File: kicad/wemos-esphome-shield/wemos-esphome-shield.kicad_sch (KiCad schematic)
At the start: 27 parts, among them Q1 2N2222, Q2 2N2222, Q3 2N2222, T1 Transformer_1P_1S, U1 WeMos_D1_mini

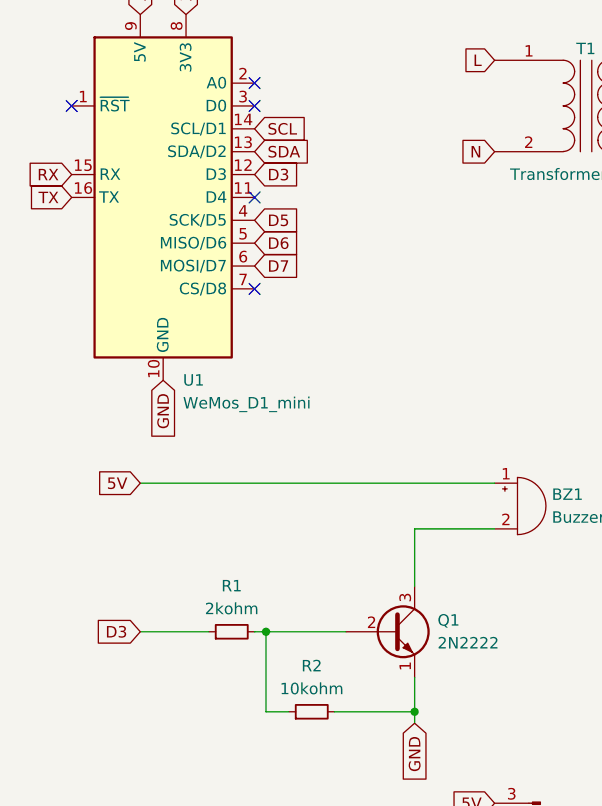
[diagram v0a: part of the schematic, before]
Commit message: reroute buzzer to D8
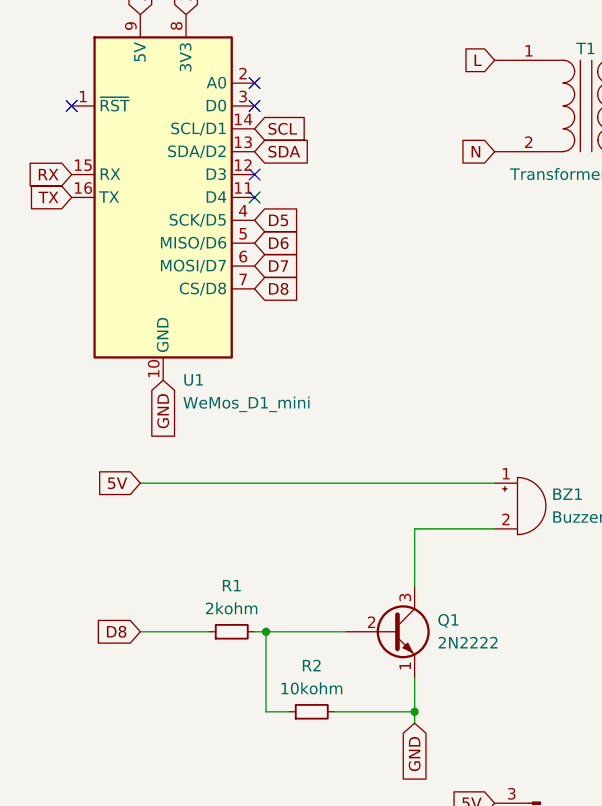
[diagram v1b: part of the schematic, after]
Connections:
- net D8: now reaches U1.7 (CS/D8)
- net D8: now also R1.1
- net D3: no longer names the net of U1.12 (D3)
- net D3: no longer R1.1
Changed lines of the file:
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@@
   (no_connect (at 55.88 40.64))
   (no_connect (at 55.88 30.48))
-  (no_connect (at 55.88 50.8))
+  (no_connect (at 55.88 38.1))
   (no_connect (at 193.04 68.58))
   (no_connect (at 193.04 55.88))
@@
     )
   )
-  (global_label "D3" (shape input) (at 55.88 38.1 0) (fields_autoplaced)
-    (effects (font (size 1.27 1.27)) (justify left))
-    (property "Intersheetrefs" "${INTERSHEET_REFS}" (at 60.7726 38.0206 0)
-      (effects (font (size 1.27 1.27)) (justify left) hide)
-    )
-  )
   (global_label "5V" (shape input) (at 193.04 24.13 180) (fields_autoplaced)
     (effects (font (size 1.27 1.27)) (justify right))
@@
     )
   )
+  (global_label "D8" (shape input) (at 55.88 50.8 0) (fields_autoplaced)
+    (effects (font (size 1.27 1.27)) (justify left))
+    (property "Intersheetrefs" "${INTERSHEET_REFS}" (at 61.3447 50.8 0)
+      (effects (font (size 1.27 1.27)) (justify left) hide)
+    )
+  )
   (global_label "D6" (shape input) (at 55.88 45.72 0) (fields_autoplaced)
     (effects (font (size 1.27 1.27)) (justify left))
@@
     )
   )
-  (global_label "D3" (shape input) (at 43.18 88.9 180) (fields_autoplaced)
-    (effects (font (size 1.27 1.27)) (justify right))
-    (property "Intersheetrefs" "${INTERSHEET_REFS}" (at 38.2874 88.8206 0)
-      (effects (font (size 1.27 1.27)) (justify right) hide)
-    )
+  (global_label "D8" (shape input) (at 43.18 88.9 180) (fields_autoplaced)
+    (effects (font (size 1.27 1.27)) (justify right))
+    (property "Intersheetrefs" "${INTERSHEET_REFS}" (at 37.7153 88.9 0)
+      (effects (font (size 1.27 1.27)) (justify right) hide)
+    )

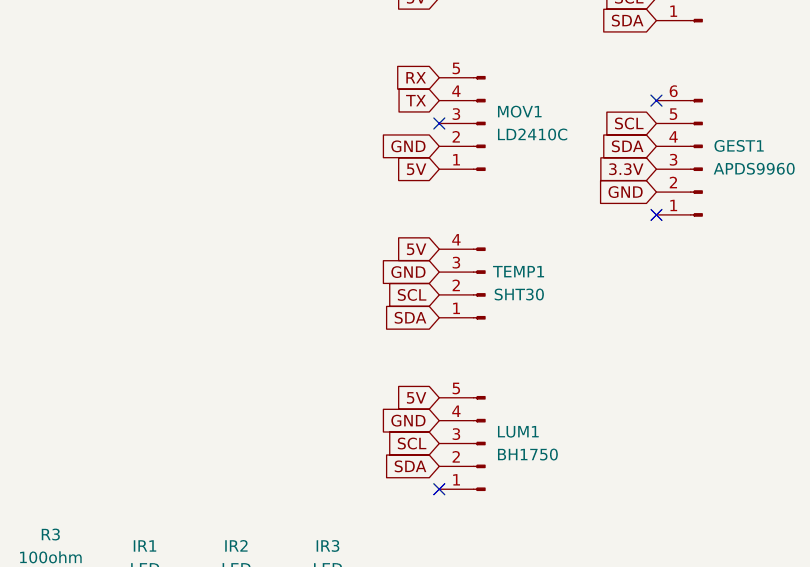
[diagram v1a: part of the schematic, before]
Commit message: move stuff around
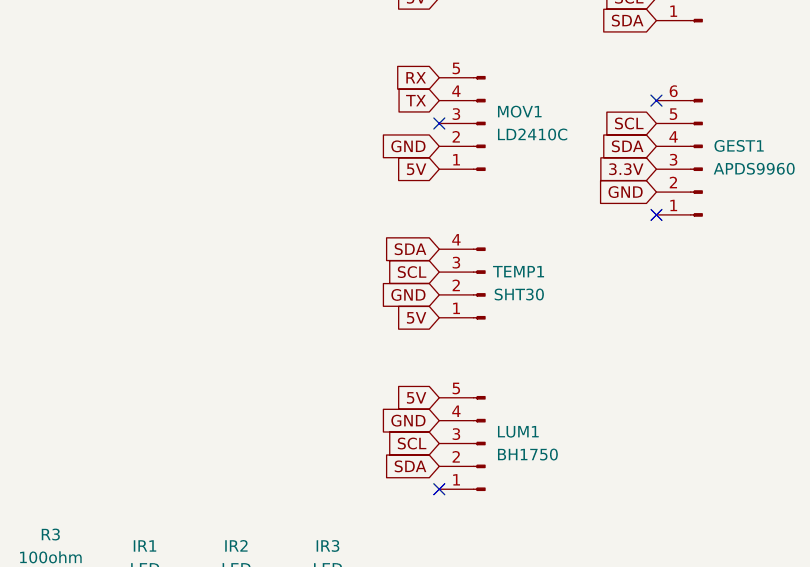
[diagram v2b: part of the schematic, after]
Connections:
- net 5V: now also TEMP1.1 (Pin_1); no longer TEMP1.4 (Pin_4)
- net GND: now also TEMP1.2 (Pin_2); no longer TEMP1.3 (Pin_3)
- net SCL: now also TEMP1.3 (Pin_3); no longer TEMP1.2 (Pin_2)
- net SDA: now also TEMP1.4 (Pin_4); no longer TEMP1.1 (Pin_1)
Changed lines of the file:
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@@
     (stroke (width 0) (type default))
   )
-  (global_label "GND" (shape input) (at 168.91 74.93 180) (fields_autoplaced)
-    (effects (font (size 1.27 1.27)) (justify right))
-    (property "Intersheetrefs" "${INTERSHEET_REFS}" (at 162.6264 74.8506 0)
+  (global_label "GND" (shape input) (at 168.91 77.47 180) (fields_autoplaced)
+    (effects (font (size 1.27 1.27)) (justify right))
+    (property "Intersheetrefs" "${INTERSHEET_REFS}" (at 162.6264 77.3906 0)
       (effects (font (size 1.27 1.27)) (justify right) hide)
     )
@@
     )
   )
-  (global_label "5V" (shape input) (at 168.91 72.39 180) (fields_autoplaced)
-    (effects (font (size 1.27 1.27)) (justify right))
-    (property "Intersheetrefs" "${INTERSHEET_REFS}" (at 164.1988 72.3106 0)
+  (global_label "5V" (shape input) (at 168.91 80.01 180) (fields_autoplaced)
+    (effects (font (size 1.27 1.27)) (justify right))
+    (property "Intersheetrefs" "${INTERSHEET_REFS}" (at 164.1988 79.9306 0)
       (effects (font (size 1.27 1.27)) (justify right) hide)
     )
@@
     )
   )
-  (global_label "SDA" (shape input) (at 168.91 80.01 180) (fields_autoplaced)
-    (effects (font (size 1.27 1.27)) (justify right))
-    (property "Intersheetrefs" "${INTERSHEET_REFS}" (at 162.9288 80.0894 0)
+  (global_label "SDA" (shape input) (at 168.91 72.39 180) (fields_autoplaced)
+    (effects (font (size 1.27 1.27)) (justify right))
+    (property "Intersheetrefs" "${INTERSHEET_REFS}" (at 162.9288 72.4694 0)
       (effects (font (size 1.27 1.27)) (justify right) hide)
     )
@@
     )
   )
-  (global_label "SCL" (shape input) (at 168.91 77.47 180) (fields_autoplaced)
-    (effects (font (size 1.27 1.27)) (justify right))
-    (property "Intersheetrefs" "${INTERSHEET_REFS}" (at 162.9893 77.5494 0)
-      (effects (font (size 1.27 1.27)) (justify right) hide)
-    )
+  (global_label "SCL" (shape input) (at 168.91 74.93 180) (fields_autoplaced)
+    (effects (font (size 1.27 1.27)) (justify right))
+    (property "Intersheetrefs" "${INTERSHEET_REFS}" (at 162.9893 75.0094 0)
+      (effects (font (size 1.27 1.27)) (justify right) hide)
+    )

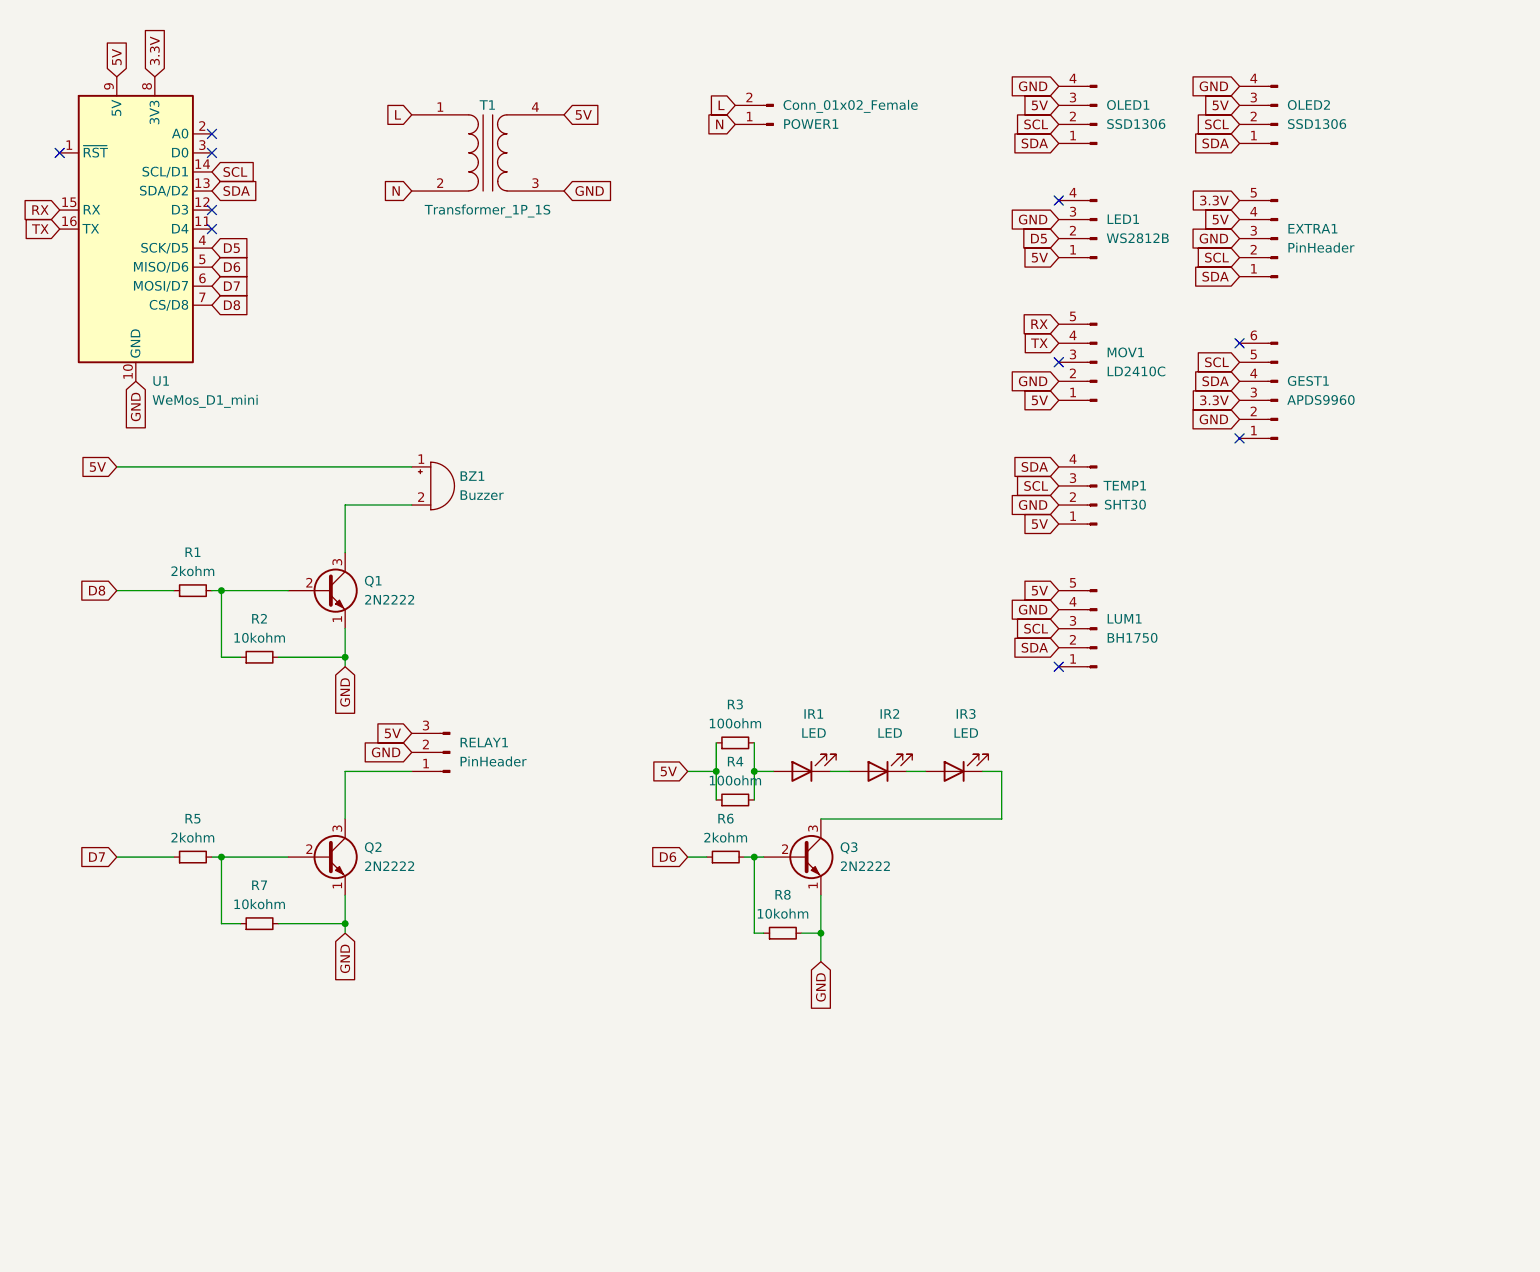
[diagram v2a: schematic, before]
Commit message: added buttons and ir receiver. rerouted everything
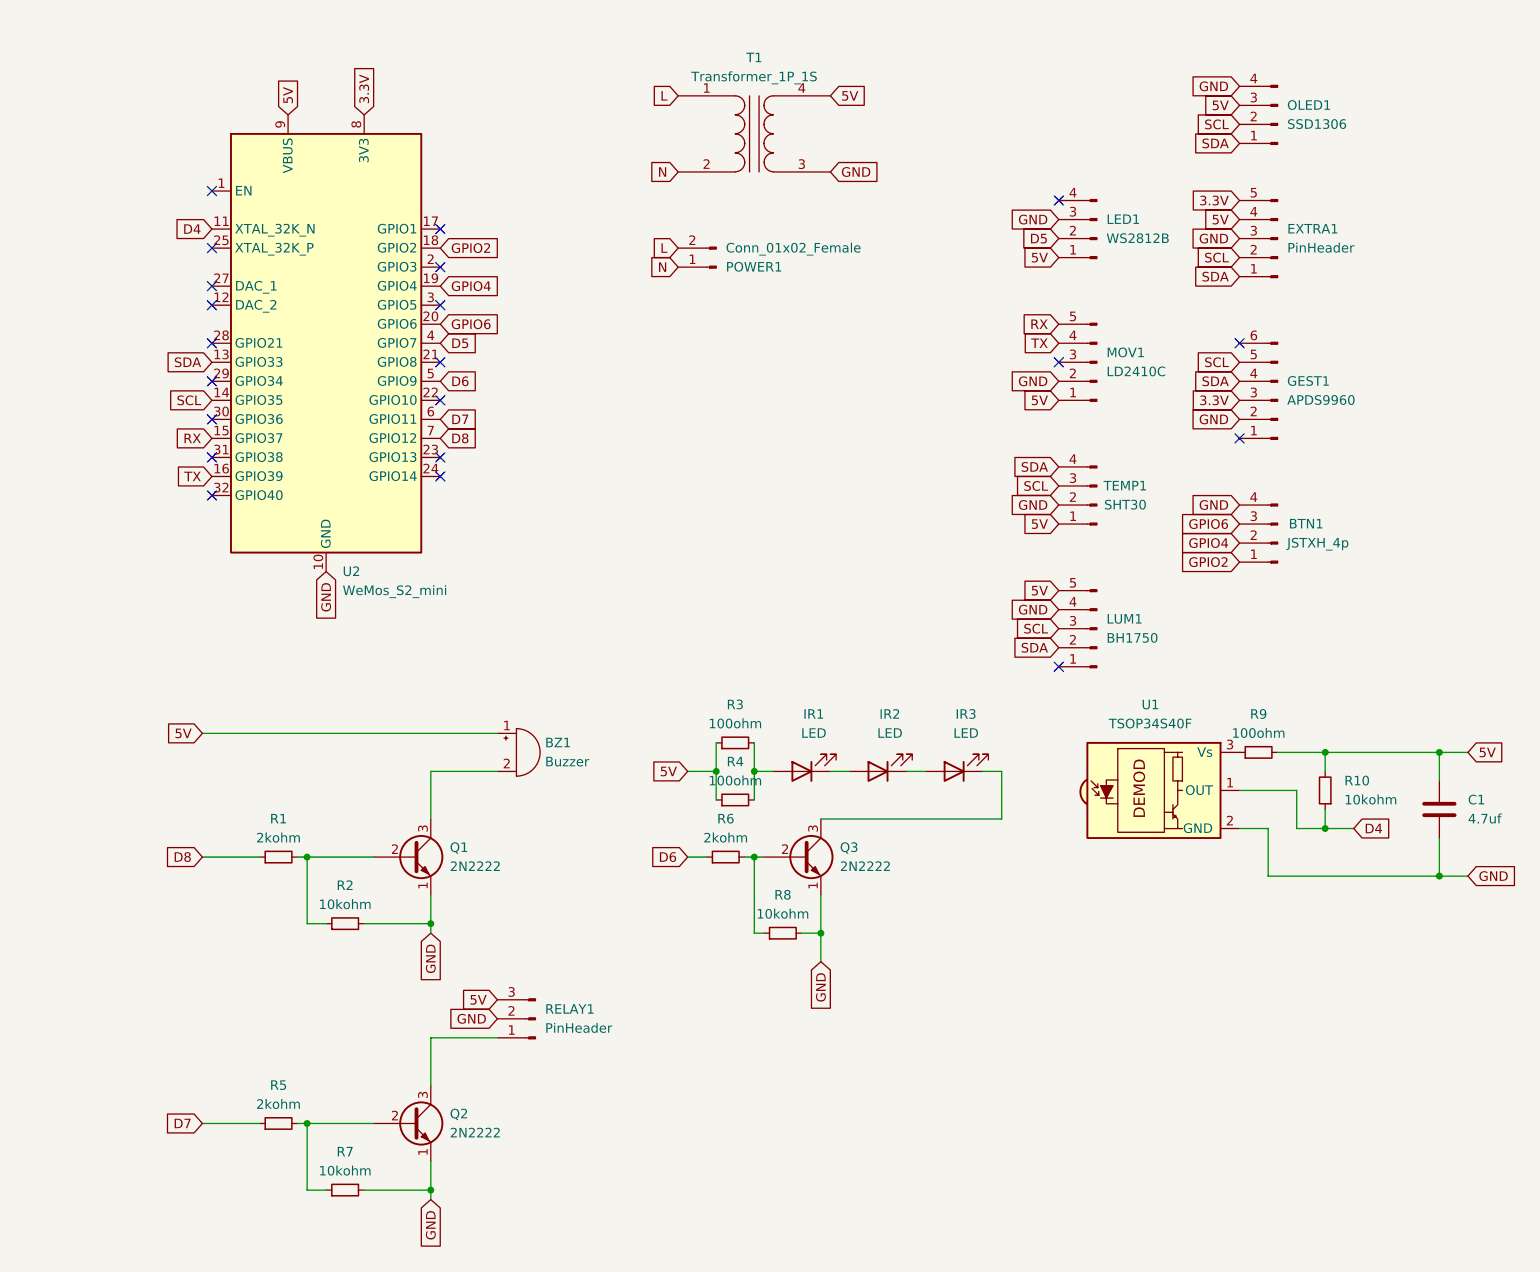
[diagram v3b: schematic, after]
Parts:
- removed OLED1: SSD1306, internal:SSD1306 OLED 128x32, symbol Connector:Conn_01x04_Pin
- removed T1: Transformer_1P_1S, internal:220v AC to 5v DC Transformer, symbol custom:Transformer_1P_1S
- removed U1: WeMos_D1_mini, Module:WEMOS_D1_mini_light, symbol MCU_Module:WeMos_D1_mini
- added BTN1: JSTXH_4p, Connector_JST:JST_XH_B4B-XH-A_1x04_P2.50mm_Vertical, symbol Connector:Conn_01x04_Pin
- added C1: 4.7uf, Capacitor_SMD:C_1206_3216Metric_Pad1.33x1.80mm_HandSolder, symbol Device:C
- added R10: 10kohm, Resistor_SMD:R_1206_3216Metric_Pad1.30x1.75mm_HandSolder, symbol Device:R_Small
- added R9: 100ohm, Resistor_SMD:R_1206_3216Metric_Pad1.30x1.75mm_HandSolder, symbol Device:R_Small
- added T1: Transformer_1P_1S, internal:220v AC to 5v DC Transformer, symbol internal:Transformer_1P_1S
- added U1: TSOP34S40F, OptoDevice:Vishay_MOLD-3Pin, symbol Interface_Optical:TSOP34S40F
- added U2: WeMos_S2_mini, internal:WEMOS_S2_mini, symbol internal:WeMos_S2_mini
- renumbered OLED2 to OLED1
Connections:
- net 3.3V: now also U2.8 (3V3)
- net 5V: now also C1.1, R10.2, R9.2, T1.4 (SB), U2.9 (VBUS)
- net D5: now also U2.4 (GPIO7)
- net D6: now also U2.5 (GPIO9)
- net D7: now also U2.6 (GPIO11)
- net D8: now also U2.7 (GPIO12)
- net GND: now also BTN1.4 (Pin_4), C1.2, T1.3 (SA), U1.2 (GND), U2.10 (GND), U2.26 (GND)
- net L: now also T1.1 (AA)
- net N: now also T1.2 (AB)
- net RX: now also U2.15 (GPIO37)
- net SCL: now also U2.14 (GPIO35)
- net SDA: now also U2.13 (GPIO33)
- net TX: now also U2.16 (GPIO39)
- new net: R9.1, U1.3 (Vs)
- new net D4: R10.1, U1.1 (OUT), U2.11 (XTAL_32K_N)
- new net GPIO2: BTN1.1 (Pin_1), U2.18 (GPIO2)
- new net GPIO4: BTN1.2 (Pin_2), U2.19 (GPIO4)
- new net GPIO6: BTN1.3 (Pin_3), U2.20 (GPIO6)
- no-connect marks 10 -> 21
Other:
- moved on the sheet: BZ1, POWER1, Q1, Q2, R1, R2, R5, R7, RELAY1

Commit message: cleanup kicad
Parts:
- removed GEST1: APDS9960, internal:APDS9960, symbol Connector:Conn_01x06_Pin
- R3, R4: value 100ohm -> 10ohm
- R6: value 2kohm -> 1kohm
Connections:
- no-connect marks 21 -> 19
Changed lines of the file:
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@@
   (no_connect (at 55.88 35.56))
   (no_connect (at 55.88 71.12))
-  (no_connect (at 193.04 68.58))
   (no_connect (at 55.88 76.2))
   (no_connect (at 55.88 60.96))
-  (no_connect (at 193.04 55.88))
   (no_connect (at 55.88 66.04))
   (no_connect (at 168.91 99.06))
@@
     )
   )
-  (global_label "GND" (shape input) (at 193.04 66.04 180) (fields_autoplaced)
-    (effects (font (size 1.27 1.27)) (justify right))
-    (property "Intersheetrefs" "${INTERSHEET_REFS}" (at 186.7564 65.9606 0)
-      (effects (font (size 1.27 1.27)) (justify right) hide)
-    )
-  )
   (global_label "D5" (shape input) (at 86.36 55.88 0) (fields_autoplaced)
     (effects (font (size 1.27 1.27)) (justify left))
@@
     )
   )
-  (global_label "3.3V" (shape input) (at 193.04 63.5 180) (fields_autoplaced)
-    (effects (font (size 1.27 1.27)) (justify right))
-    (property "Intersheetrefs" "${INTERSHEET_REFS}" (at 185.9424 63.5 0)
-      (effects (font (size 1.27 1.27)) (justify right) hide)
-    )
-  )
   (global_label "SCL" (shape input) (at 193.04 26.67 180) (fields_autoplaced)
     (effects (font (size 1.27 1.27)) (justify right))
@@
     )
   )
-  (global_label "SCL" (shape input) (at 193.04 58.42 180) (fields_autoplaced)
-    (effects (font (size 1.27 1.27)) (justify right))
-    (property "Intersheetrefs" "${INTERSHEET_REFS}" (at 187.1193 58.4994 0)
-      (effects (font (size 1.27 1.27)) (justify right) hide)
-    )
-  )
   (global_label "GND" (shape input) (at 85.09 134.62 270) (fields_autoplaced)
     (effects (font (size 1.27 1.27)) (justify right))
@@
     (effects (font (size 1.27 1.27)) (justify right))
     (property "Intersheetrefs" "${INTERSHEET_REFS}" (at 49.8988 107.8706 0)
-      (effects (font (size 1.27 1.27)) (justify right) hide)
-    )
-  )
-  (global_label "SDA" (shape input) (at 193.04 60.96 180) (fields_autoplaced)
-    (effects (font (size 1.27 1.27)) (justify right))
-    (property "Intersheetrefs" "${INTERSHEET_REFS}" (at 187.0588 61.0394 0)
       (effects (font (size 1.27 1.27)) (justify right) hide)
     )
@@
     )
   )
-  (symbol (lib_id "Connector:Conn_01x06_Pin") (at 198.12 63.5 180) (unit 1)
-    (in_bom yes) (on_board yes) (dnp no) (fields_autoplaced)
-    (property "Reference" "GEST1" (at 199.39 60.96 0)
-      (effects (font (size 1.27 1.27)) (justify right))
-    )
-    (property "Value" "APDS9960" (at 199.39 63.5 0)
-      (effects (font (size 1.27 1.27)) (justify right))
-    )
-    (property "Footprint" "internal:APDS9960" (at 198.12 63.5 0)
-      (effects (font (size 1.27 1.27)) hide)
-    )
-    (property "Datasheet" "~" (at 198.12 63.5 0)
-      (effects (font (size 1.27 1.27)) hide)
-    )
-    (pin "6")
-    (pin "1")
-    (pin "5")
-    (pin "2")
-    (pin "3")
-    (pin "4")
-    (instances
-      (project "wemos-esphome-shield"
-        (path "/c86a51bd-2371-491c-bb3a-3b240c2028f6"
-          (reference "GEST1") (unit 1)
-        )
-      )
-    )
-  )
   (symbol (lib_id "Device:R_Small") (at 204.47 115.57 180) (unit 1)
     (in_bom yes) (on_board yes) (dnp no) (fields_autoplaced)
@@
       (effects (font (size 1.27 1.27)))
     )
-    (property "Value" "2kohm" (at 124.46 121.92 90)
+    (property "Value" "1kohm" (at 124.46 121.92 90)
       (effects (font (size 1.27 1.27)))
     )
@@
       (effects (font (size 1.27 1.27)))
     )
-    (property "Value" "100ohm" (at 125.73 106.68 90)
+    (property "Value" "10ohm" (at 125.73 106.68 90)
       (effects (font (size 1.27 1.27)))
     )
@@
       (effects (font (size 1.27 1.27)))
     )
-    (property "Value" "100ohm" (at 125.73 114.3 90)
-      (effects (font (size 1.27 1.27)))
-    )
+    (property "Value" "10ohm" (at 125.73 114.3 90)
+      (effects (font (size 1.27 1.27)))
+    )
